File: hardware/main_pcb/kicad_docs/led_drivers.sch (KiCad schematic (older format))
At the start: 9 parts, among them U5 MCP6004, U6 DG469EQ, U7 DG469EQ

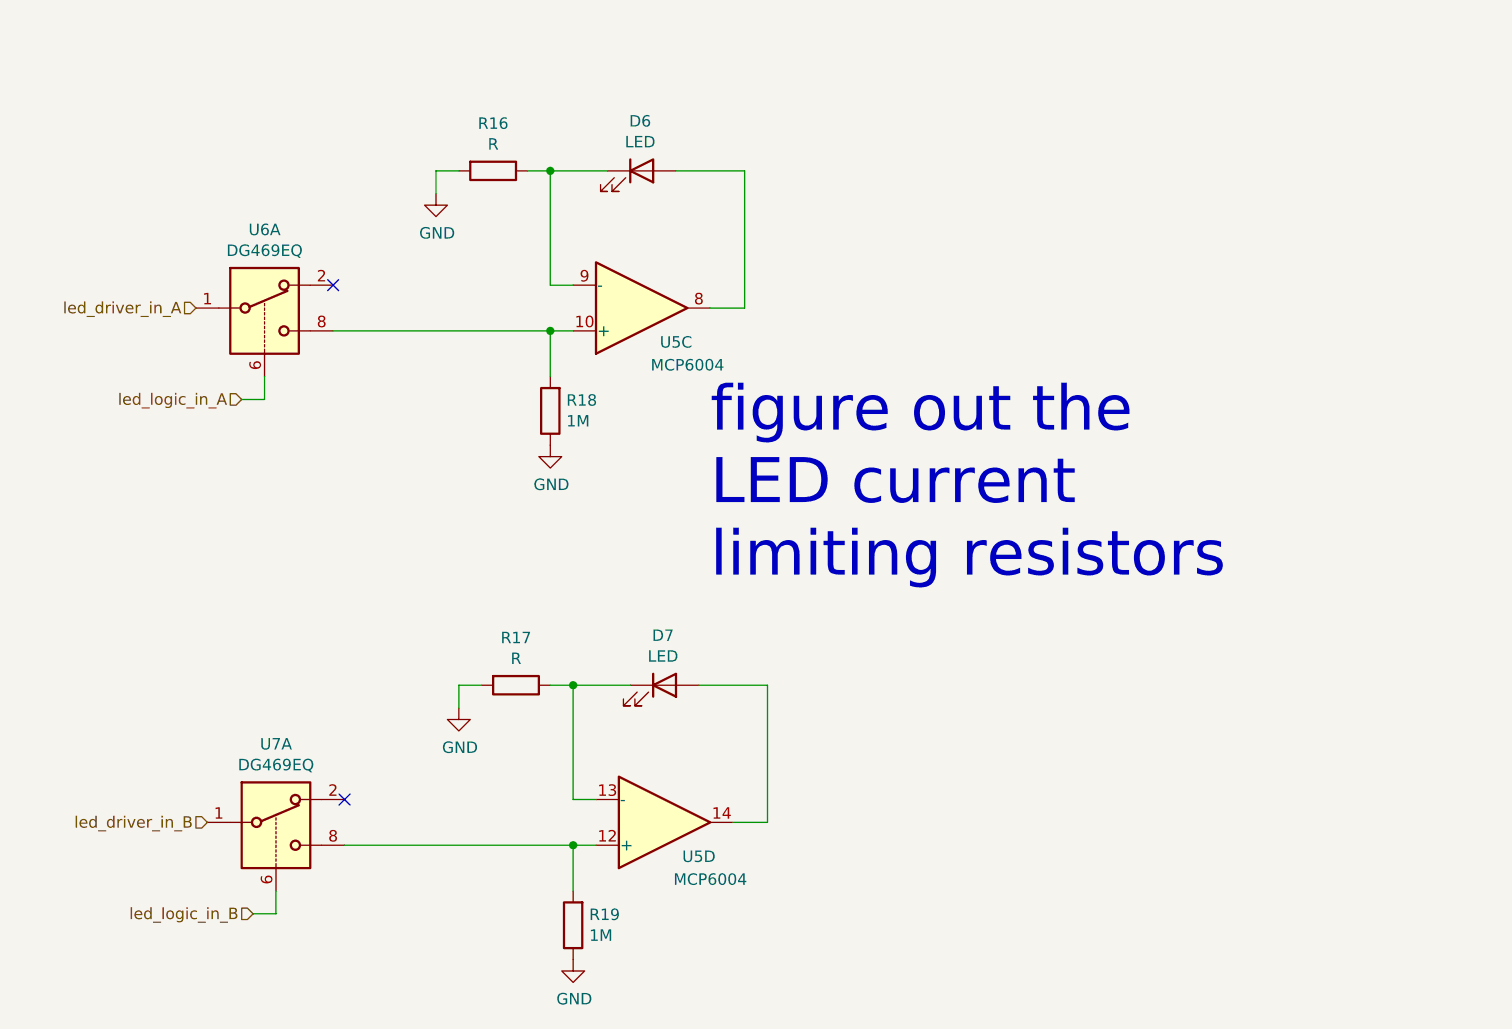
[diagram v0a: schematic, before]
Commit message: reduce analog switch count, tidy up
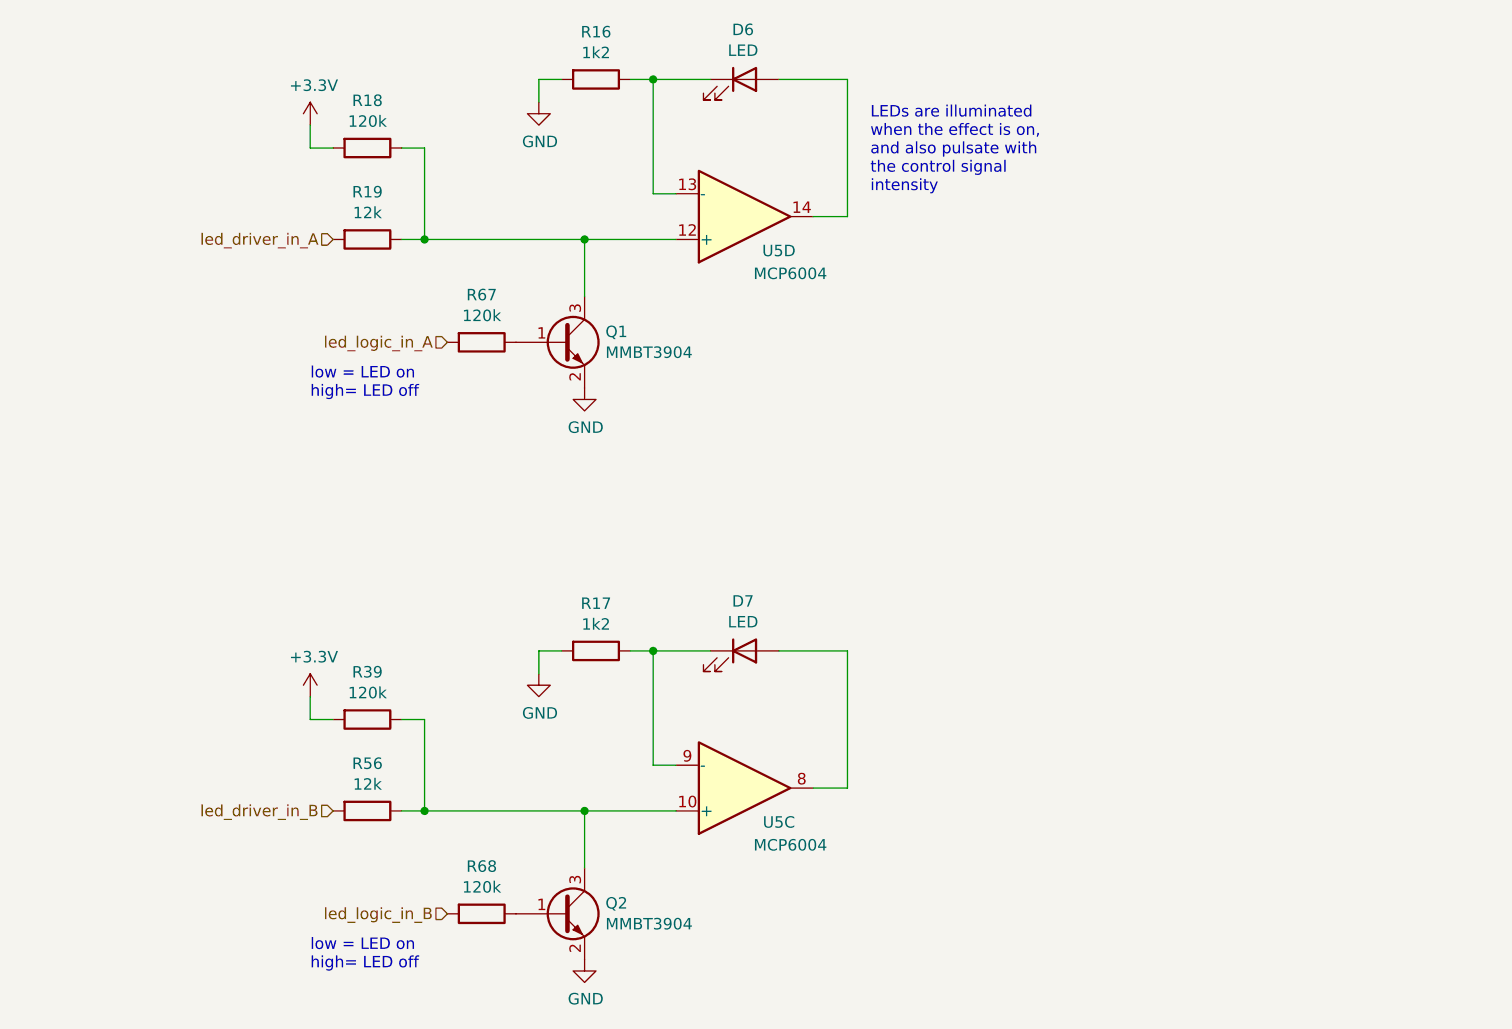
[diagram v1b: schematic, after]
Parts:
- removed U6, U7: DG469EQ, Package_SO:MSOP-8_3x3mm_P0.65mm, symbol custom_components:DG469EQ
- added Q1, Q2: MMBT3904, Package_TO_SOT_SMD:SOT-23, symbol Transistor_BJT:MMBT3904
- added R39, R67, R68: 120k, Resistor_SMD:R_0603_1608Metric, symbol Device:R
- added R56: 12k, Resistor_SMD:R_0603_1608Metric, symbol Device:R
- R16, R17: value R -> 1k2
- R18: value 1M -> 120k
- R19: value 1M -> 12k
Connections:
- net GND: now also Q1.2 (E), Q2.2 (E); no longer R18.1, R19.1
- net led_driver_in_A: now also R19.2
- net led_driver_in_B: now also R56.2
- net led_logic_in_A: now also R67.2
- net led_logic_in_B: now also R68.2
- net at U5.10 (+): now also Q2.3 (C), R39.1, R56.1; no longer R18.2
- net at U5.8: now also D7.2 (A); no longer D6.2 (A)
- net at D6.1 (K), R16.1: now also U5.13 (-); no longer U5.9 (-)
- net at U5.12 (+): now also R18.1, R19.1, Q1.3 (C); no longer R19.2
- net at D7.1 (K), R17.1: now also U5.9 (-); no longer U5.13 (-)
- net at U5.14: now also D6.2 (A); no longer D7.2 (A)
- new net: Q1.1 (B), R67.1
- new net: Q2.1 (B), R68.1
- new net +3V3: R18.2, R39.2
- no-connect marks 2 -> 0
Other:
- note added: "LEDs are illuminated\nwhen the effect is on,\nand also pulsate with\nthe control signal\nintensity"
- note added: "low = LED on\nhigh= LED off"
- note removed: "figure out the \nLED current \nlimiting resistors"
- moved on the sheet: D6, D7, R16, R17, U5C, U5D
